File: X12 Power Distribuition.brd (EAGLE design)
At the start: 152.4 x 76.2 mm, 43 parts, among them Q1 SPB80P06P, Y1 ECS-80-S-4X

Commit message: worked on board
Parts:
- moved D4 114.3 mm to (34.3, 10.2)
- moved R3 111.3 mm to (31.8, 15.2), flipped to the bottom, turned to 180 degrees
- moved J2 95.3 mm to (16.5, 5.08)
- moved J1 90.2 mm to (6.35, 5.08)
- moved Q1 85.8 mm to (20.3, 30.5)
- moved J4 79.2 mm to (5.08, 71.1)
- moved J3 76.9 mm to (14.0, 71.1)
- moved D2 13.3 mm to (8.89, 90.2)
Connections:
- removed net ALERT_A: U$5.31
- removed net ALERT_B: U$7.31
- removed net CLK_A: U$5.30
- removed net CLK_B: U$7.30
- removed net DATA_A: U$5.32
- removed net DATA_B: U$7.32
- new net ALERT: U$4.PB7, U$5.31, U$7.31
- new net CLK: U$4.PA9, U$5.30, U$7.30
- new net DATA: U$4.PA10, U$5.32, U$7.32
- net +48V: now also J3.P$1
- net +48V_RAW: no longer J3.P$1
- net 3V3GND: now also SV1.3
- net GND: no longer SV1.3
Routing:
- net N$3: track 0.00 -> 34.1 mm, vias 0 -> 1
- added copper zone on layer 1, net +12V_A
- added copper zone on layer 1, net +12V_B
- added copper zone on layer 16, net 48V_GND

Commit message: Started Board Placement
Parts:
- moved C11 170.7 mm to (141.0, 17.8), turned to 270 degrees
- moved R6 158.9 mm to (125.5, 53.3), turned to 270 degrees
- moved U$8 158.9 mm to (135.9, 24.6)
- moved R5 152.6 mm to (116.6, 42.4), turned to 90 degrees
- moved C10 147.9 mm to (123.4, 27.4), turned to 90 degrees
- moved C9 138.4 mm to (116.6, 29.5), turned to 270 degrees
- moved C4 133.5 mm to (137.2, 39.1), turned to 270 degrees
- moved C8 131.7 mm to (111.5, 29.5), turned to 270 degrees
- moved R10 129.6 mm to (148.6, 17.8), turned to 90 degrees
- moved R11 129.6 mm to (144.8, 17.8), turned to 270 degrees
- moved C2 124.6 mm to (133.3, 39.1), turned to 270 degrees
- moved C7 122.2 mm to (121.9, 53.3), turned to 270 degrees
- moved Y1 112.0 mm to (114.0, 37.3)
- moved C6 110.2 mm to (105.9, 47.0), turned to 90 degrees
- moved C5 109.8 mm to (109.2, 47.0), turned to 90 degrees
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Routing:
- net 3V3GND: track 0.00 -> 50.5 mm
- net +3V3: track 0.00 -> 49.8 mm
- net ALERT: track 0.00 -> 43.0 mm, vias 0 -> 1
- net NRST: track 0.00 -> 19.2 mm
- net OSC_IN: track 0.00 -> 11.4 mm
- net CAN_L: track 0.00 -> 11.3 mm
- net N$6: track 0.00 -> 11.3 mm
- net N$7: track 0.00 -> 11.3 mm
- net N$5: track 0.00 -> 7.62 mm
- net OSC_OUT: track 0.00 -> 5.90 mm
- net CAN_H: track 0.00 -> 5.55 mm

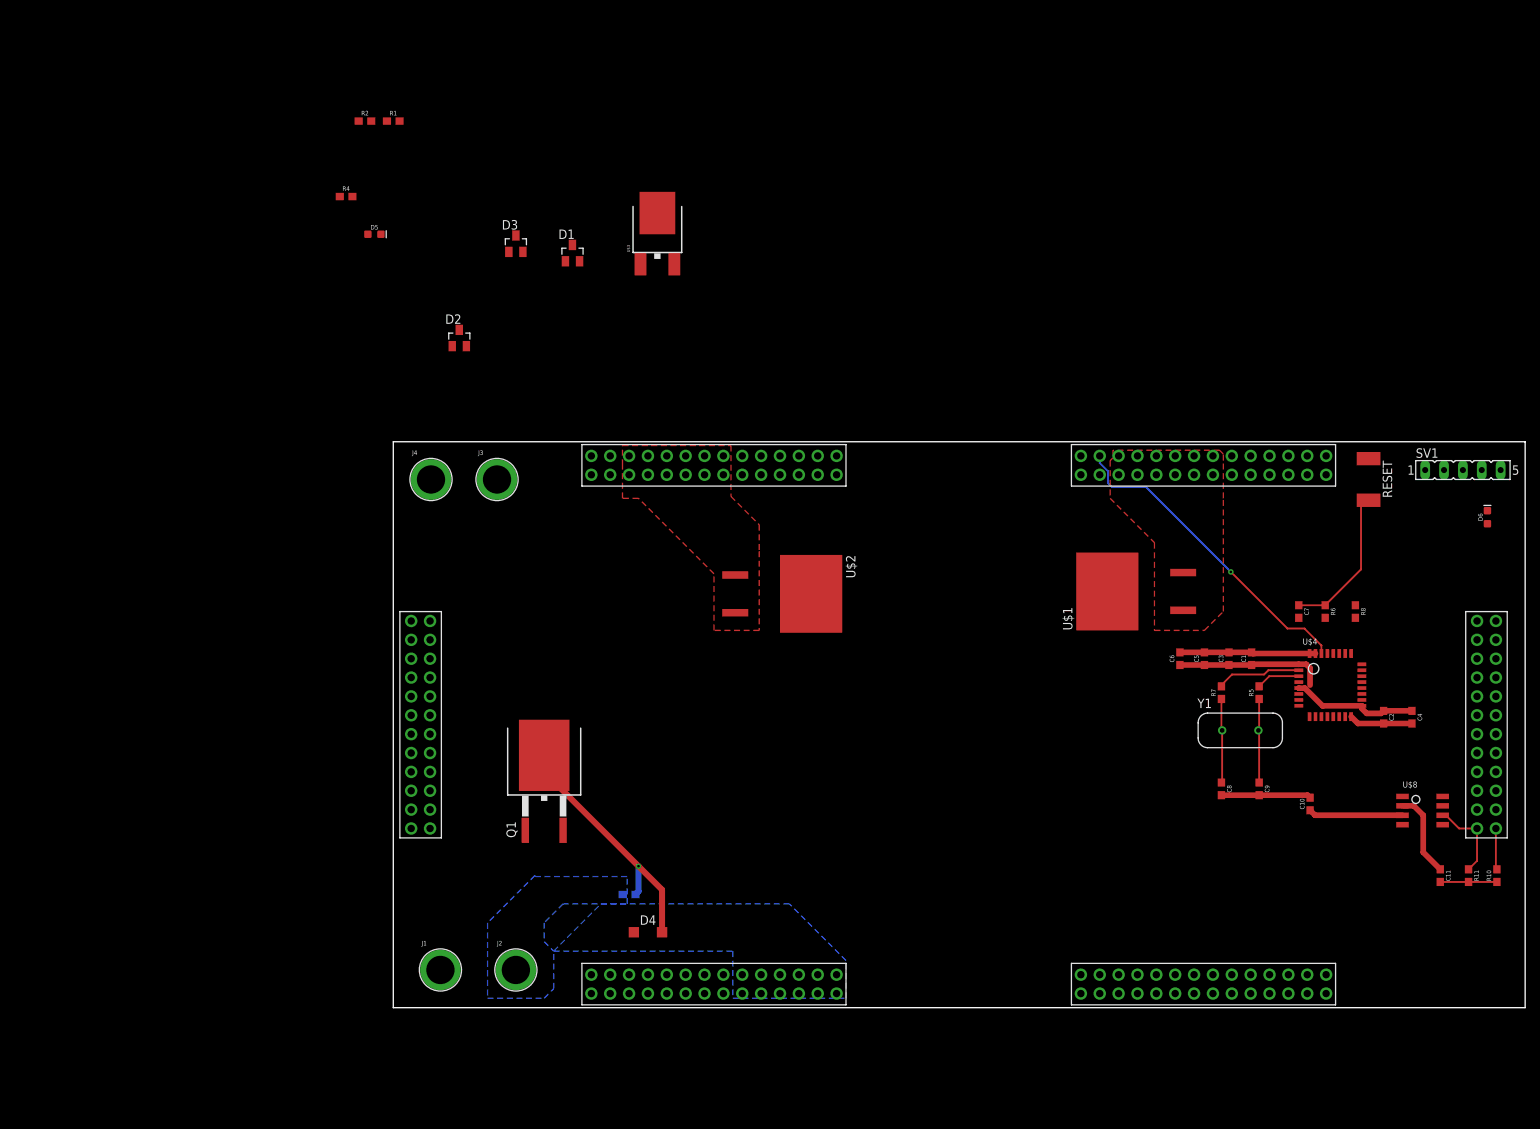
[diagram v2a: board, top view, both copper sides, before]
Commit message: updated connector
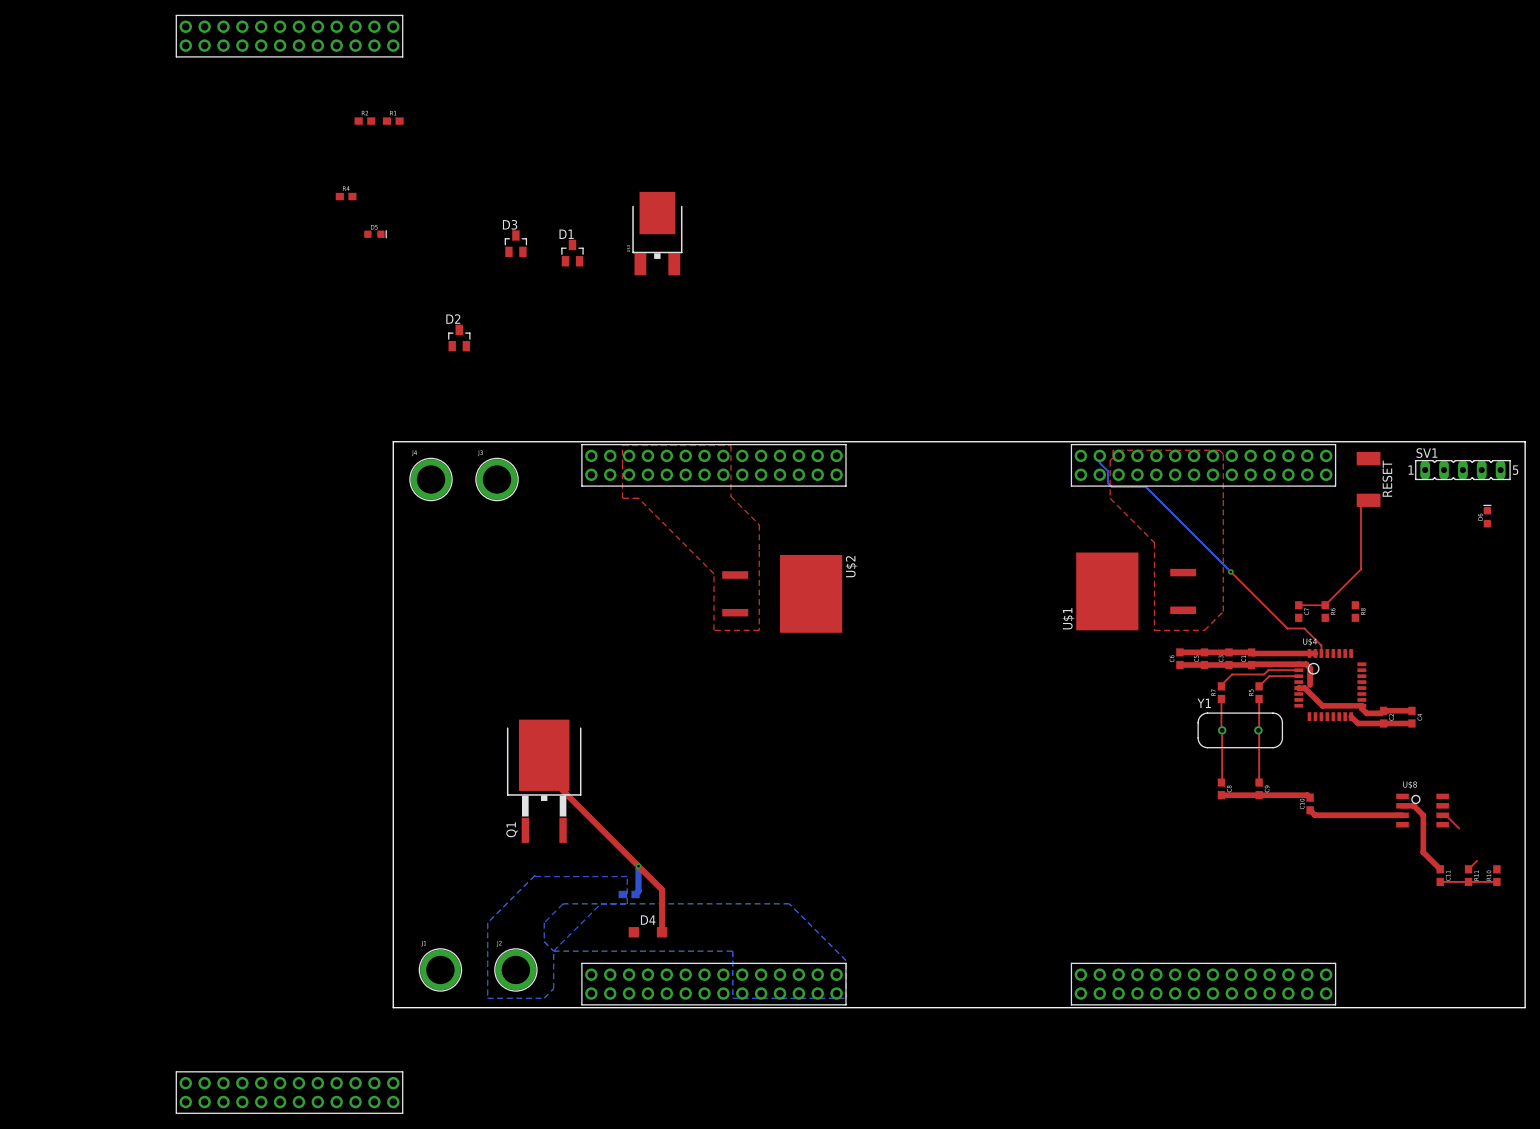
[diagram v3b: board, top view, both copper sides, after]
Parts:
- moved U$6 59.8 mm to (-27.9, -12.7), turned to 0 degrees
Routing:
- net CAN_L: track 11.3 -> 4.57 mm
- net CAN_H: track 5.55 -> 0.18 mm

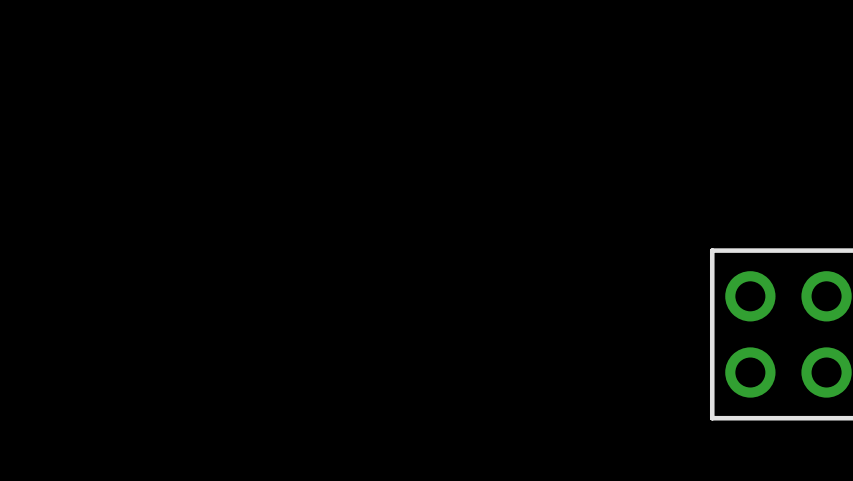
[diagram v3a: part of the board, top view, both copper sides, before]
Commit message: added standoffs
added the standoffs to the board
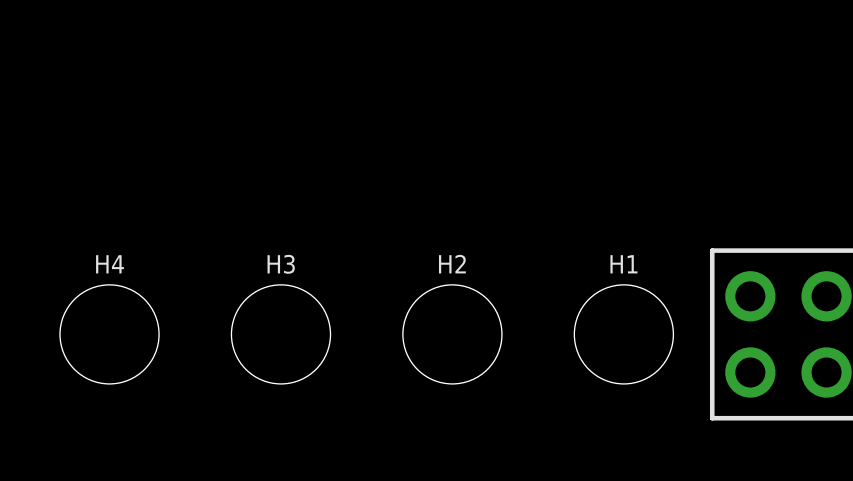
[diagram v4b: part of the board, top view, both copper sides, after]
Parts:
- added H1, H2, H3, H4: STAND-OFF, SparkFun-Hardware:STAND-OFF
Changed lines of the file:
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@@
 <element name="U$5" library="Dist_to_Brickboard_Connector" package="BRICKBOARD_TSW_14X2" value="BRICKBOARD_TSW_14X2" x="109.093" y="3.175"/>
 <element name="U$6" library="Dist_to_Conversion_Connector" package="CONVERSION_TSW_12X2" value="CONVERSION_TSW_12X2" x="-27.94" y="-12.7"/>
+<element name="H1" library="SparkFun-Hardware" library_urn="urn:adsk.eagle:library:519" package="STAND-OFF" package3d_urn="urn:adsk.eagle:package:38630/1" value="STAND-OFF" x="-32.1564" y="-11.43">
+<attribute name="NAME" x="-32.1564" y="-9.398" size="0.6096" layer="25" font="vector" ratio="20" align="bottom-center"/>
+<attribute name="VALUE" x="-32.1564" y="-13.462" size="0.6096" layer="27" font="vector" ratio="20" align="top-center"/>
+</element>
+<element name="H2" library="SparkFun-Hardware" library_urn="urn:adsk.eagle:library:519" package="STAND-OFF" package3d_urn="urn:adsk.eagle:package:38630/1" value="STAND-OFF" x="-37.8714" y="-11.43">
+<attribute name="NAME" x="-37.8714" y="-9.398" size="0.6096" layer="25" font="vector" ratio="20" align="bottom-center"/>
+<attribute name="VALUE" x="-37.8714" y="-13.462" size="0.6096" layer="27" font="vector" ratio="20" align="top-center"/>
+</element>
+<element name="H3" library="SparkFun-Hardware" library_urn="urn:adsk.eagle:library:519" package="STAND-OFF" package3d_urn="urn:adsk.eagle:package:38630/1" value="STAND-OFF" x="-43.5864" y="-11.43">
+<attribute name="NAME" x="-43.5864" y="-9.398" size="0.6096" layer="25" font="vector" ratio="20" align="bottom-center"/>
+<attribute name="VALUE" x="-43.5864" y="-13.462" size="0.6096" layer="27" font="vector" ratio="20" align="top-center"/>
+</element>
+<element name="H4" library="SparkFun-Hardware" library_urn="urn:adsk.eagle:library:519" package="STAND-OFF" package3d_urn="urn:adsk.eagle:package:38630/1" value="STAND-OFF" x="-49.3014" y="-11.43">
+<attribute name="NAME" x="-49.3014" y="-9.398" size="0.6096" layer="25" font="vector" ratio="20" align="bottom-center"/>
+<attribute name="VALUE" x="-49.3014" y="-13.462" size="0.6096" layer="27" font="vector" ratio="20" align="top-center"/>
+</element>
 </elements>
 <signals>

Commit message: Board
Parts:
- moved U$6 73.5 mm to (4.32, 53.3), turned to 270 degrees
- moved J4 0.94 mm to (6.02, 71.1)
